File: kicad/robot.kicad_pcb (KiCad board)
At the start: 2 copper layers, 67.6 x 59.8 mm, 76 parts, among them J1 Adafruit Coil Jumper, J2 Adafruit Coil Jumper, J3 Adafruit Coil Jumper, J4 Adafruit Coil Jumper, M5 Motor_DC, M6 Motor_DC, M7 Motor_DC, M8 Motor_DC, Q2 NMOS, U10 GY-521, U13 DRV8833PW, U6 DRV8833PW, U8 ESP32-DEVKITC, U9 MCP73831-2-OT

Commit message: Make schematic pretty
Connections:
- net Net-(U8-IO21) renamed /Temporary/Controller/SDA
- net Net-(U8-IO22) renamed /Temporary/Controller/SCL
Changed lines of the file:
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@@
   (net 51 "Net-(U8-IO5)")
   (net 52 "unconnected-(U8-GND2-Pad32)")
-  (net 53 "Net-(U8-IO21)")
+  (net 53 "/Temporary/Controller/SDA")
   (net 54 "unconnected-(U8-RXD0-Pad34)")
   (net 55 "unconnected-(U8-TXD0-Pad35)")
-  (net 56 "Net-(U8-IO22)")
+  (net 56 "/Temporary/Controller/SCL")
   (net 57 "unconnected-(U10-PadXDA)")
   (net 58 "unconnected-(U10-PadXCL)")
@@
   (net 73 "Net-(U8-IO35)")
   (net 74 "unconnected-(U8-IO0-Pad25)")
-  (footprint "Resistor_SMD:R_0805_2012Metric_Pad1.20x1.40mm_HandSolder" (layer "F.Cu")
-    (at 212.4 83.2 90)
-    (descr "Resistor SMD 0805 (2012 Metric), square (rectangular) end terminal, IPC_7351 nominal with elongated pad for handsoldering. (Body size source: IPC-SM-782 page 72, https://www.pcb-3d.com/wordpress/wp-content/uploads/ipc-sm-782a_amendment_1_and_2.pdf), generated with kicad-footprint-generator")
-    (tags "resistor handsolder")
-    (property "Sheetfile" "controller.kicad_sch")
-    (property "Sheetname" "Controller")
-    (property "ki_description" "Resistor")
-    (property "ki_keywords" "R res resistor")
-    (attr smd)
-    (fp_text reference "R14" (at 0 -1.65 90) (layer "F.SilkS")
-        (effects (font (size 1 1) (thickness 0.15)))
-    )
-    (fp_text value "10k" (at 0 1.65 90) (layer "F.Fab")
-        (effects (font (size 1 1) (thickness 0.15)))
-    )
-    (fp_text user "${REFERENCE}" (at 0 0 90) (layer "F.Fab")
-        (effects (font (size 0.5 0.5) (thickness 0.08)))
-    )
-    (fp_line (start -0.227064 -0.735) (end 0.227064 -0.735)
-      (stroke (width 0.12) (type solid)) (layer "F.SilkS"))
-    (fp_line (start -0.227064 0.735) (end 0.227064 0.735)
-      (stroke (width 0.12) (type solid)) (layer "F.SilkS"))
-    (fp_line (start -1.85 -0.95) (end 1.85 -0.95)
-      (stroke (width 0.05) (type solid)) (layer "F.CrtYd"))
-    (fp_line (start -1.85 0.95) (end -1.85 -0.95)
-      (stroke (width 0.05) (type solid)) (layer "F.CrtYd"))
-    (fp_line (start 1.85 -0.95) (end 1.85 0.95)
-      (stroke (width 0.05) (type solid)) (layer "F.CrtYd"))
-    (fp_line (start 1.85 0.95) (end -1.85 0.95)
-      (stroke (width 0.05) (type solid)) (layer "F.CrtYd"))
-    (fp_line (start -1 -0.625) (end 1 -0.625)
-      (stroke (width 0.1) (type solid)) (layer "F.Fab"))
-    (fp_line (start -1 0.625) (end -1 -0.625)
-      (stroke (width 0.1) (type solid)) (layer "F.Fab"))
-    (fp_line (start 1 -0.625) (end 1 0.625)
-      (stroke (width 0.1) (type solid)) (layer "F.Fab"))
-    (fp_line (start 1 0.625) (end -1 0.625)
-      (stroke (width 0.1) (type solid)) (layer "F.Fab"))
-    (pad "1" smd roundrect (at -1 0 90) (size 1.2 1.4) (layers "F.Cu" "F.Paste" "F.Mask") (roundrect_rratio 0.208333)
-      (net 73 "Net-(U8-IO35)") (pintype "passive"))
-    (pad "2" smd roundrect (at 1 0 90) (size 1.2 1.4) (layers "F.Cu" "F.Paste" "F.Mask") (roundrect_rratio 0.208333)
-      (net 62 "/Temporary/Controller/GND") (pintype "passive"))
-    (model "${KICAD6_3DMODEL_DIR}/Resistor_SMD.3dshapes/R_0805_2012Metric.wrl"
-      (offset (xyz 0 0 0))
-      (scale (xyz 1 1 1))
-      (rotate (xyz 0 0 0))
-    )
-  )
   (footprint "Fuse:Fuse_0805_2012Metric_Pad1.15x1.40mm_HandSolder" (layer "F.Cu")
     (at 206.2 58.775 90)
@@
     )
   )
+  (footprint "Resistor_SMD:R_0805_2012Metric_Pad1.20x1.40mm_HandSolder" (layer "F.Cu")
+    (at 212.4 83.2 90)
+    (descr "Resistor SMD 0805 (2012 Metric), square (rectangular) end terminal, IPC_7351 nominal with elongated pad for handsoldering. (Body size source: IPC-SM-782 page 72, https://www.pcb-3d.com/wordpress/wp-content/uploads/ipc-sm-782a_amendment_1_and_2.pdf), generated with kicad-footprint-generator")
+    (tags "resistor handsolder")
+    (property "Sheetfile" "controller.kicad_sch")
+    (property "Sheetname" "Controller")
+    (property "ki_description" "Resistor")
+    (property "ki_keywords" "R res resistor")
+    (attr smd)
+    (fp_text reference "R14" (at 0 -1.65 90) (layer "F.SilkS")
+        (effects (font (size 1 1) (thickness 0.15)))
+    )
+    (fp_text value "10k" (at 0 1.65 90) (layer "F.Fab")
+        (effects (font (size 1 1) (thickness 0.15)))
+    )
+    (fp_text user "${REFERENCE}" (at 0 0 90) (layer "F.Fab")
+        (effects (font (size 0.5 0.5) (thickness 0.08)))
+    )
+    (fp_line (start -0.227064 -0.735) (end 0.227064 -0.735)
+      (stroke (width 0.12) (type solid)) (layer "F.SilkS"))
+    (fp_line (start -0.227064 0.735) (end 0.227064 0.735)
+      (stroke (width 0.12) (type solid)) (layer "F.SilkS"))
+    (fp_line (start -1.85 -0.95) (end 1.85 -0.95)
+      (stroke (width 0.05) (type solid)) (layer "F.CrtYd"))
+    (fp_line (start -1.85 0.95) (end -1.85 -0.95)
+      (stroke (width 0.05) (type solid)) (layer "F.CrtYd"))
+    (fp_line (start 1.85 -0.95) (end 1.85 0.95)
+      (stroke (width 0.05) (type solid)) (layer "F.CrtYd"))
+    (fp_line (start 1.85 0.95) (end -1.85 0.95)
+      (stroke (width 0.05) (type solid)) (layer "F.CrtYd"))
+    (fp_line (start -1 -0.625) (end 1 -0.625)
+      (stroke (width 0.1) (type solid)) (layer "F.Fab"))
+    (fp_line (start -1 0.625) (end -1 -0.625)
+      (stroke (width 0.1) (type solid)) (layer "F.Fab"))
+    (fp_line (start 1 -0.625) (end 1 0.625)
+      (stroke (width 0.1) (type solid)) (layer "F.Fab"))
+    (fp_line (start 1 0.625) (end -1 0.625)
+      (stroke (width 0.1) (type solid)) (layer "F.Fab"))
+    (pad "1" smd roundrect (at -1 0 90) (size 1.2 1.4) (layers "F.Cu" "F.Paste" "F.Mask") (roundrect_rratio 0.208333)
+      (net 73 "Net-(U8-IO35)") (pintype "passive"))
+    (pad "2" smd roundrect (at 1 0 90) (size 1.2 1.4) (layers "F.Cu" "F.Paste" "F.Mask") (roundrect_rratio 0.208333)
+      (net 62 "/Temporary/Controller/GND") (pintype "passive"))
+    (model "${KICAD6_3DMODEL_DIR}/Resistor_SMD.3dshapes/R_0805_2012Metric.wrl"
+      (offset (xyz 0 0 0))
+      (scale (xyz 1 1 1))
+      (rotate (xyz 0 0 0))
+    )
+  )
   (footprint "GY-521:GY-521" (layer "F.Cu")
     (at 216.69 75.45)
@@
       (net 60 "unconnected-(U10-PadINT)") (pinfunction "INT") (pintype "bidirectional+no_connect") (solder_mask_margin 0.102))
     (pad "SCL" thru_hole oval (at -8.89 -3.81) (size 3.556 1.778) (drill 0.8) (layers "*.Cu" "*.Mask")
-      (net 56 "Net-(U8-IO22)") (pinfunction "SCL") (pintype "bidirectional") (solder_mask_margin 0.102))
+      (net 56 "/Temporary/Controller/SCL") (pinfunction "SCL") (pintype "bidirectional") (solder_mask_margin 0.102))
     (pad "SDA" thru_hole oval (at -8.89 -1.27) (size 3.556 1.778) (drill 0.8) (layers "*.Cu" "*.Mask")
-      (net 53 "Net-(U8-IO21)") (pinfunction "SDA") (pintype "bidirectional") (solder_mask_margin 0.102))
+      (net 53 "/Temporary/Controller/SDA") (pinfunction "SDA") (pintype "bidirectional") (solder_mask_margin 0.102))
     (pad "VCC" thru_hole oval (at -8.89 -8.89) (size 3.556 1.778) (drill 0.8) (layers "*.Cu" "*.Mask")
       (net 66 "/Temporary/Controller/3V3") (pinfunction "VCC") (pintype "bidirectional") (solder_mask_margin 0.102))
@@
       (net 52 "unconnected-(U8-GND2-Pad32)") (pinfunction "GND2") (pintype "power_in+no_connect") (solder_mask_margin 0.102))
     (pad "33" thru_hole circle (at 12.7 -10.15) (size 1.53 1.53) (drill 1.02) (layers "*.Cu" "*.Mask")
-      (net 53 "Net-(U8-IO21)") (pinfunction "IO21") (pintype "bidirectional") (solder_mask_margin 0.102))
+      (net 53 "/Temporary/Controller/SDA") (pinfunction "IO21") (pintype "bidirectional") (solder_mask_margin 0.102))
     (pad "34" thru_hole circle (at 12.7 -12.69) (size 1.53 1.53) (drill 1.02) (layers "*.Cu" "*.Mask")
       (net 54 "unconnected-(U8-RXD0-Pad34)") (pinfunction "RXD0") (pintype "input+no_connect") (solder_mask_margin 0.102))
@@
       (net 55 "unconnected-(U8-TXD0-Pad35)") (pinfunction "TXD0") (pintype "output+no_connect") (solder_mask_margin 0.102))
     (pad "36" thru_hole circle (at 12.7 -17.77) (size 1.53 1.53) (drill 1.02) (layers "*.Cu" "*.Mask")
-      (net 56 "Net-(U8-IO22)") (pinfunction "IO22") (pintype "bidirectional") (solder_mask_margin 0.102))
+      (net 56 "/Temporary/Controller/SCL") (pinfunction "IO22") (pintype "bidirectional") (solder_mask_margin 0.102))
     (pad "37" thru_hole circle (at 12.7 -20.31) (size 1.53 1.53) (drill 1.02) (layers "*.Cu" "*.Mask")
       (net 38 "Net-(U13-BIN1)") (pinfunction "IO23") (pintype "bidirectional") (solder_mask_margin 0.102))

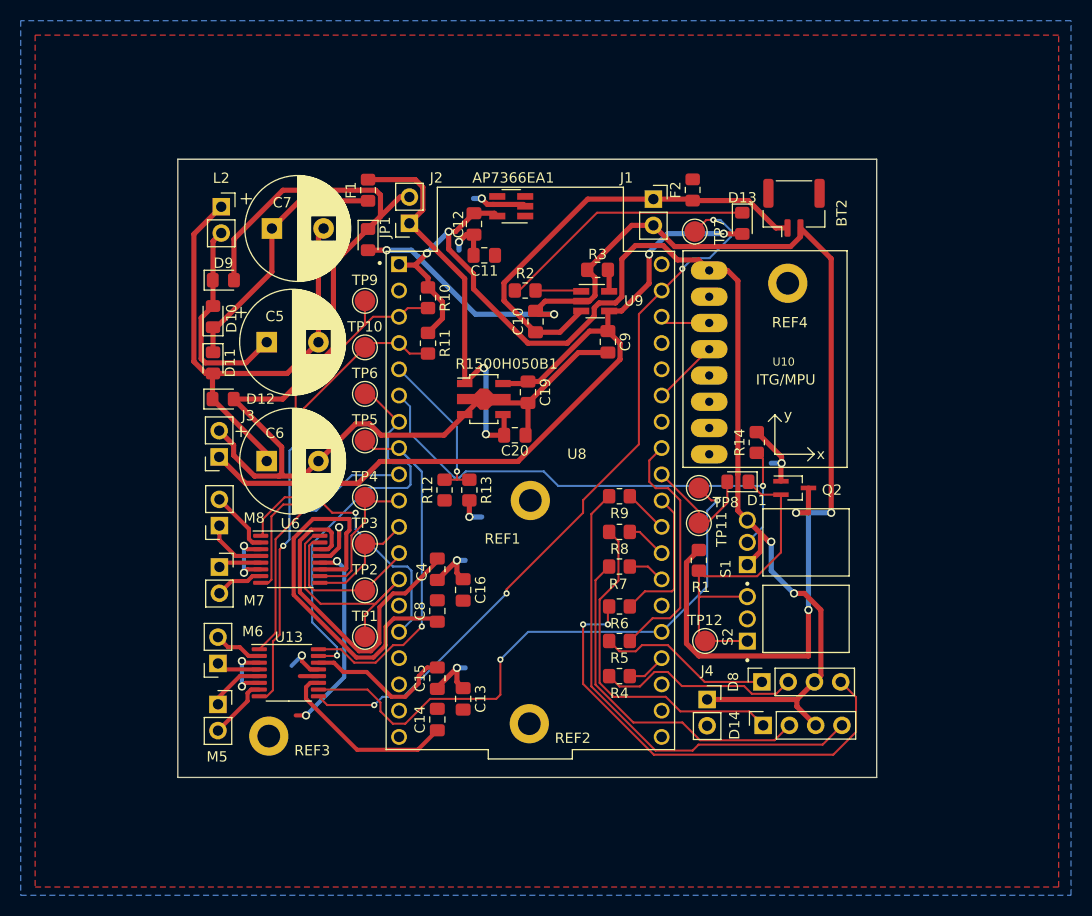
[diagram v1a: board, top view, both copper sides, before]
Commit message: Cleaned up ground traces
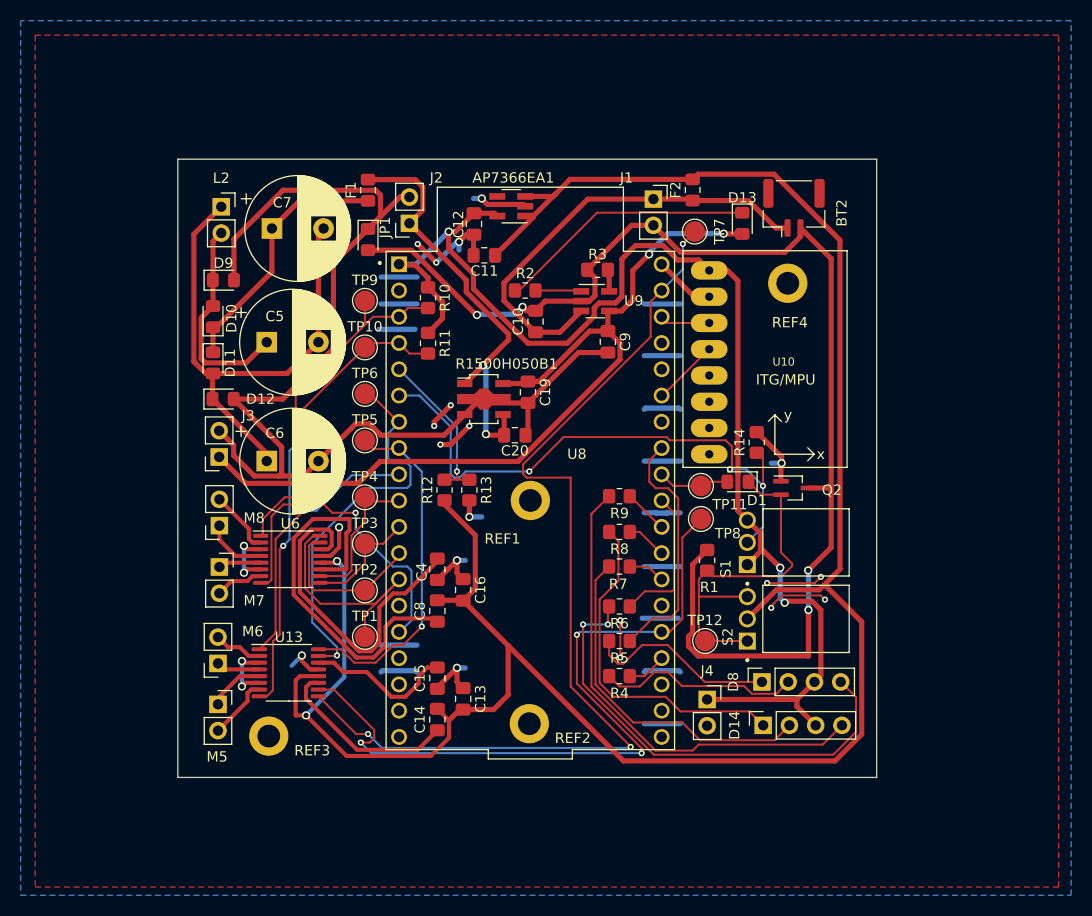
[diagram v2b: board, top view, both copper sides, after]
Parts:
- moved TP11 3.61 mm to (207.0, 87.4)
- moved TP8 3.01 mm to (207.0, 90.6)
- moved R1 0.80 mm to (207.6, 94.6)
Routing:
- net /Temporary/Controller/VBAT: track 21.3 -> 218.1 mm
- net /Temporary/Controller/GND: track 52.3 -> 134.2 mm, vias 12 -> 24
- net Net-(U13-BIN1): track 72.4 -> 95.8 mm, vias 4 -> 3
- net Net-(U13-BIN2): track 58.0 -> 72.2 mm, vias 2 -> 3
- net Net-(BT2--): track 127.6 -> 121.2 mm, vias 5 -> 4
- net Net-(U8-IO35): track 50.6 -> 56.1 mm, vias 1 -> 3
- net /Temporary/Controller/MOSTRIG: track 12.5 -> 7.62 mm
- net Net-(J2-Pin_1): track 40.2 -> 44.0 mm
- net /Temporary/Controller/3V3: track 123.1 -> 125.7 mm, vias 4 -> 3
- net Net-(D1-K): track 34.2 -> 36.0 mm
- net Net-(D8-GK): track 16.9 -> 18.7 mm

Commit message: Fix MOSFET footprint pinout
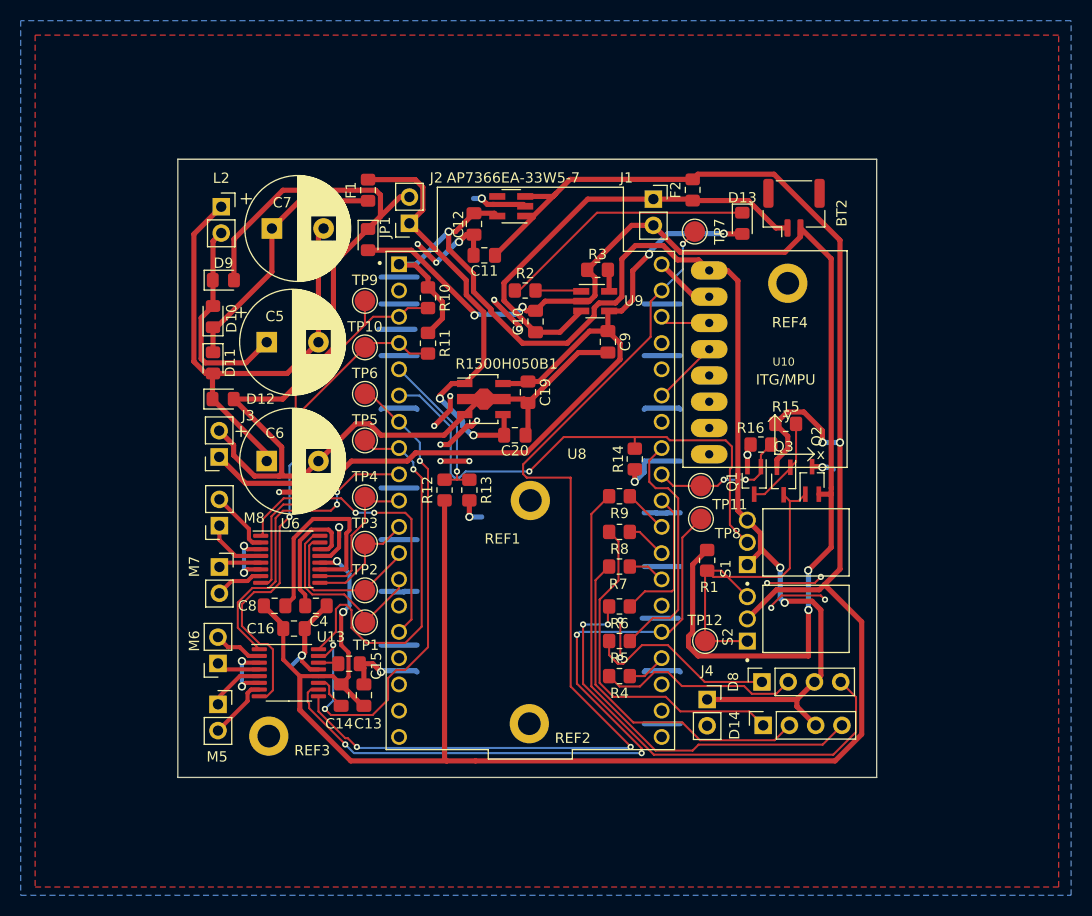
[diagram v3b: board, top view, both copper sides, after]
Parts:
- removed D1: D, Diode_SMD:D_0805_2012Metric_Pad1.15x1.40mm_HandSolder
- added Q1: NMOS, Package_TO_SOT_SMD:SOT-323_SC-70_Handsoldering, F.Cu at (212.2, 86.9)
- added Q3: PMOS, Package_TO_SOT_SMD:SOT-323_SC-70_Handsoldering, F.Cu at (215.0, 86.9)
- added R15: 10k, Resistor_SMD:R_0805_2012Metric_Pad1.20x1.40mm_HandSolder, F.Cu at (215.2, 81.4)
- added R16: 10k, Resistor_SMD:R_0805_2012Metric_Pad1.20x1.40mm_HandSolder, F.Cu at (212.8, 83.4)
- moved C16 16.8 mm to (167.6, 101.2), turned to 180 degrees
- moved C8 15.7 mm to (165.8, 99.0), turned to 180 degrees
- moved C4 12.3 mm to (169.8, 99.0), turned to 180 degrees
- moved R14 11.9 mm to (200.6, 84.8), turned to -90 degrees
- moved C13 9.61 mm to (174.4, 107.6)
- moved C14 9.60 mm to (172.2, 107.6)
- moved C15 8.65 mm to (173.0, 104.6), turned to 180 degrees
- moved Q2 1.83 mm to (217.8, 86.9), turned to 90 degrees
- moved TP1 1.40 mm to (174.5, 100.6)
- renumbered AP7366EA1 to AP7366EA-33W5-7
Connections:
- Q2 pad 1: /Temporary/Controller/GND -> Net-(Q2-G)
- Q2 pad 2: Net-(D1-K) -> Net-(BT2--)
- Q2 pad 3: Net-(BT2--) -> /Temporary/Controller/GND
- R1 pad 1: Net-(D1-K) -> Net-(Q2-G)
- S2 pad 1: Net-(D1-K) -> Net-(Q2-G)
- S2 pad 3: Net-(D1-K) -> Net-(Q2-G)
- TP12 pad 1: Net-(D1-K) -> Net-(Q2-G)
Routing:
- net Net-(D1-K): track 36.0 -> 0.00 mm
- net Net-(Q2-G): track 0.00 -> 33.6 mm
- net /Temporary/Controller/GND: track 134.2 -> 162.1 mm, vias 24 -> 31
- net Net-(U6-VINT): track 32.7 -> 12.7 mm
- net Net-(U6-VCP): track 38.3 -> 20.5 mm
- net Net-(U13-VCP): track 18.0 -> 3.57 mm
- net /Temporary/Controller/VBAT: track 218.1 -> 232.4 mm, vias 2 -> 4
- net Net-(U13-VINT): track 14.5 -> 1.96 mm
- net Net-(U13-AIN2): track 38.1 -> 50.1 mm, vias 1 -> 3
- net Net-(Q1-D): track 0.00 -> 9.06 mm
- net /Temporary/Controller/MOSTRIG: track 7.62 -> 15.0 mm, vias 0 -> 2
- net Net-(U8-IO35): track 56.1 -> 51.3 mm, vias 3 -> 1
- net Net-(U13-nSLEEP): track 25.8 -> 30.4 mm, vias 1 -> 2
- net Net-(U6-AIN1): track 23.6 -> 19.1 mm
- net Net-(U13-nFAULT): track 45.1 -> 49.4 mm
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
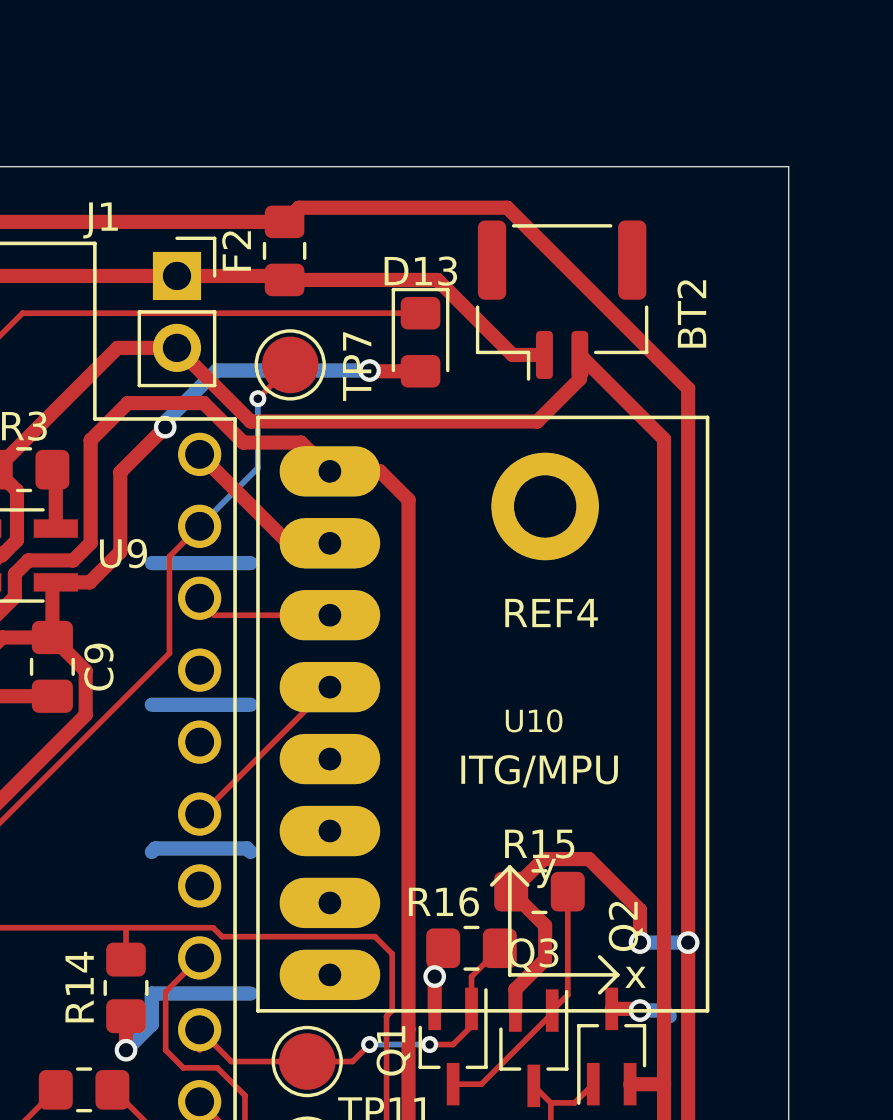
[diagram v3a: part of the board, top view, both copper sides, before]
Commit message: Change battery connector
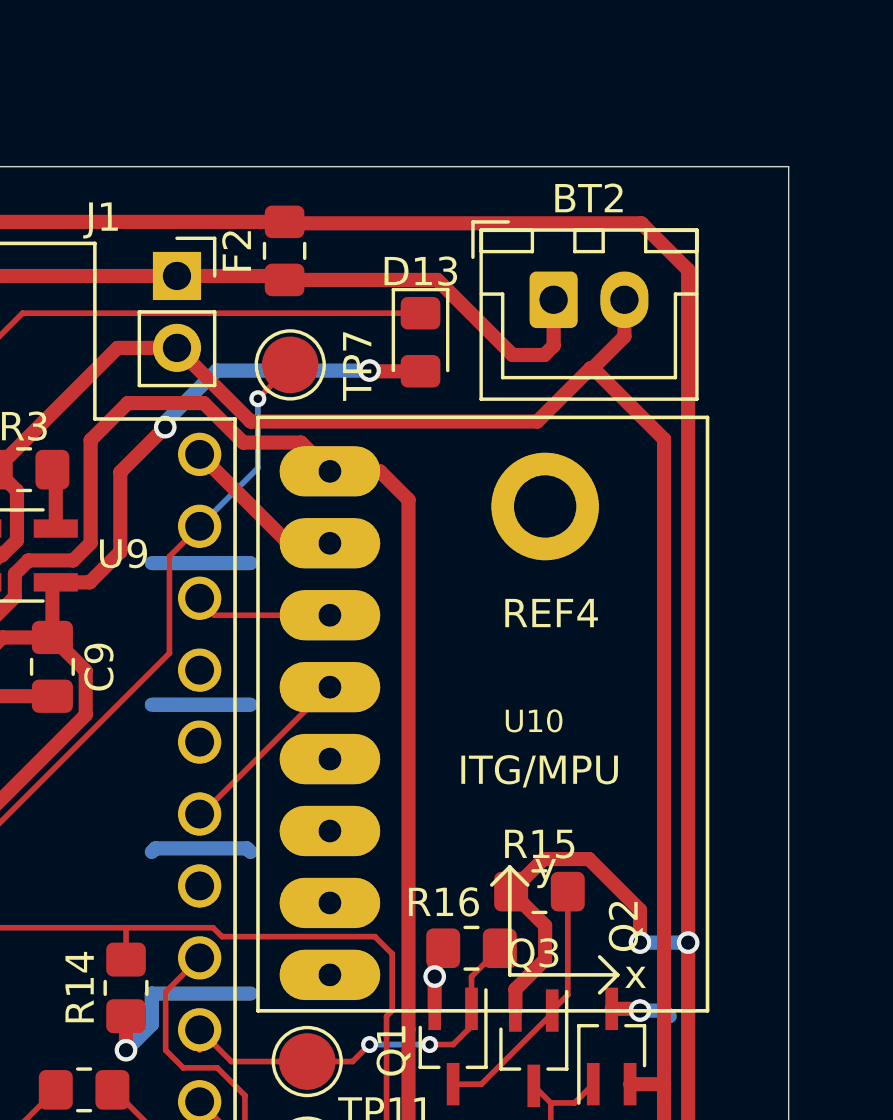
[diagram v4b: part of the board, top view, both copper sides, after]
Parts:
- BT2: footprint Connector_JST:JST_GH_BM02B-GHS-TBT_1x02-1MP_P1.25mm_Vertical -> Connector_JST:JST_XH_B2B-XH-A_1x02_P2.50mm_Vertical
- moved BT2 0.30 mm to (215.7, 60.5)
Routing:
- net Net-(BT2-+): track 43.2 -> 45.3 mm
- net /Temporary/Controller/VBAT: track 232.4 -> 234.4 mm
- net Net-(BT2--): track 120.4 -> 122.4 mm

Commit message: Final PCB
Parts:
- AP7366EA-33W5-7: value ~ -> AP7366EA-33W5-7
- D10, D11, D12, D9: value D -> SD0805S020S1R0
- D13: value LED -> LTST-C171GKT
- D14, D8: value LED_RGBA -> QBL8RGB60D0-2897
- F1: value Fuse -> MFU0805FF01000P100
- F2: value Fuse -> MFU0805FF03000P100
- Q1, Q2: value NMOS -> DMG1012UW-7
- Q3: value PMOS -> DMG1013UW-7
- R1500H050B1: value ~ -> R1500H050B1
- moved REF2 0.60 mm to (190.4, 109.8)
- moved REF1 0.59 mm to (190.5, 89.4)
- moved C6 0.40 mm to (165.4, 85.0)
- moved REF4 0.20 mm to (215.4, 67.6)
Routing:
- net Net-(D12-A): track 112.8 -> 114.5 mm
